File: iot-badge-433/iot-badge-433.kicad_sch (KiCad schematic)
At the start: 70 parts, among them J1 USB_C_Receptacle_USB2.0, J2 Wire ANT, J3 Conn_01x04_Male, Q1 BC847, Q2 BC847, SW1 SW_Push, SW2 SW_Push, SW3 SW_Push, SW4 SW_Push, SW5 SW_Push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

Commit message: added resistors to sw to protect against shorts
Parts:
- added R21, R22: 220, Resistor_SMD:R_0805_2012Metric_Pad1.20x1.40mm_HandSolder, symbol Device:R
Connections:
- net SW5-32: now also R21.2; no longer SW5.1
- net SW6-33: now also R22.2; no longer SW6.1
- new net: R21.1, SW5.1
- new net: R22.1, SW6.1
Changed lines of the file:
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@@
     (stroke (width 0) (type default) (color 0 0 0 0))
   )
-  (wire (pts (xy 259.08 157.48) (xy 269.24 157.48))
-    (stroke (width 0) (type default) (color 0 0 0 0))
-  )
   (wire (pts (xy 21.59 55.88) (xy 21.59 57.15))
     (stroke (width 0) (type default) (color 0 0 0 0))
@@
     (stroke (width 0) (type default) (color 0 0 0 0))
   )
+  (wire (pts (xy 259.08 157.48) (xy 260.35 157.48))
+    (stroke (width 0) (type default) (color 0 0 0 0))
+  )
   (wire (pts (xy 43.18 170.18) (xy 58.42 170.18))
     (stroke (width 0) (type default) (color 0 0 0 0))
@@
     (stroke (width 0) (type default) (color 0 0 0 0))
   )
-  (wire (pts (xy 259.08 146.05) (xy 269.24 146.05))
-    (stroke (width 0) (type default) (color 0 0 0 0))
-  )
   (wire (pts (xy 29.21 44.45) (xy 29.21 45.72))
     (stroke (width 0) (type default) (color 0 0 0 0))
@@
     (stroke (width 0) (type default) (color 0 0 0 0))
   )
+  (wire (pts (xy 259.08 146.05) (xy 260.35 146.05))
+    (stroke (width 0) (type default) (color 0 0 0 0))
+  )
   (wire (pts (xy 205.74 157.48) (xy 205.74 158.75))
     (stroke (width 0) (type default) (color 0 0 0 0))
@@
     (stroke (width 0) (type default) (color 0 0 0 0))
   )
+  (wire (pts (xy 267.97 157.48) (xy 269.24 157.48))
+    (stroke (width 0) (type default) (color 0 0 0 0))
+  )
   (wire (pts (xy 250.19 34.29) (xy 254 34.29))
     (stroke (width 0) (type default) (color 0 0 0 0))
@@
     (stroke (width 0) (type default) (color 0 0 0 0))
   )
+  (wire (pts (xy 267.97 146.05) (xy 269.24 146.05))
+    (stroke (width 0) (type default) (color 0 0 0 0))
+  )
   (wire (pts (xy 147.32 176.53) (xy 147.32 167.64))
     (stroke (width 0) (type default) (color 0 0 0 0))
@@
     (pin "2")
   )
+  (symbol (lib_id "Device:R") (at 264.16 157.48 270) (unit 1)
+    (in_bom yes) (on_board yes) (fields_autoplaced)
+    (property "Reference" "R22" (id 0) (at 264.16 151.13 90))
+    (property "Value" "220" (id 1) (at 264.16 153.67 90))
+    (property "Footprint" "Resistor_SMD:R_0805_2012Metric_Pad1.20x1.40mm_HandSolder" (id 2) (at 264.16 155.702 90)
+      (effects (font (size 1.27 1.27)) hide)
+    )
+    (property "Datasheet" "~" (id 3) (at 264.16 157.48 0)
+      (effects (font (size 1.27 1.27)) hide)
+    )
+    (pin "1")
+    (pin "2")
+  )
   (symbol (lib_id "power:Earth") (at 205.74 158.75 0) (unit 1)
     (in_bom yes) (on_board yes) (fields_autoplaced)
@@
     (pin "2")
   )
+  (symbol (lib_id "Device:R") (at 264.16 146.05 270) (unit 1)
+    (in_bom yes) (on_board yes) (fields_autoplaced)
+    (property "Reference" "R21" (id 0) (at 264.16 139.7 90))
+    (property "Value" "220" (id 1) (at 264.16 142.24 90))
+    (property "Footprint" "Resistor_SMD:R_0805_2012Metric_Pad1.20x1.40mm_HandSolder" (id 2) (at 264.16 144.272 90)
+      (effects (font (size 1.27 1.27)) hide)
+    )
+    (property "Datasheet" "~" (id 3) (at 264.16 146.05 0)
+      (effects (font (size 1.27 1.27)) hide)
+    )
+    (pin "1")
+    (pin "2")
+  )
   (symbol (lib_id "Device:LED") (at 266.7 69.85 90) (unit 1)
     (in_bom yes) (on_board yes)
@@
       (reference "R20") (unit 1) (value "20k") (footprint "Resistor_SMD:R_0805_2012Metric_Pad1.20x1.40mm_HandSolder")
     )
+    (path "/a94d6832-7d1d-42d9-9422-eb0ac2cf6b62"
+      (reference "R21") (unit 1) (value "220") (footprint "Resistor_SMD:R_0805_2012Metric_Pad1.20x1.40mm_HandSolder")
+    )
+    (path "/1cb6b24c-a887-45f3-a8f4-72a5085c9147"
+      (reference "R22") (unit 1) (value "220") (footprint "Resistor_SMD:R_0805_2012Metric_Pad1.20x1.40mm_HandSolder")
+    )
     (path "/0c62dc8b-b218-44e3-b535-1d9d37793c70"

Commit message: added resistor to switch
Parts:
- added R23: 220, Resistor_SMD:R_0805_2012Metric_Pad1.20x1.40mm_HandSolder, symbol Device:R
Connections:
- net SW4-17: now also R23.2; no longer SW4.1
- new net: R23.1, SW4.1
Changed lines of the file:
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@@
     (stroke (width 0) (type default) (color 0 0 0 0))
   )
+  (wire (pts (xy 226.06 157.48) (xy 227.33 157.48))
+    (stroke (width 0) (type default) (color 0 0 0 0))
+  )
   (wire (pts (xy 43.18 170.18) (xy 58.42 170.18))
     (stroke (width 0) (type default) (color 0 0 0 0))
@@
     (stroke (width 0) (type default) (color 0 0 0 0))
   )
-  (wire (pts (xy 217.17 157.48) (xy 227.33 157.48))
-    (stroke (width 0) (type default) (color 0 0 0 0))
-  )
   (wire (pts (xy 181.61 72.39) (xy 181.61 77.47))
     (stroke (width 0) (type default) (color 0 0 0 0))
@@
     (stroke (width 0) (type default) (color 0 0 0 0))
   )
+  (wire (pts (xy 217.17 157.48) (xy 218.44 157.48))
+    (stroke (width 0) (type default) (color 0 0 0 0))
+  )
   (wire (pts (xy 259.08 146.05) (xy 260.35 146.05))
     (stroke (width 0) (type default) (color 0 0 0 0))
@@
     (pin "3")
   )
+  (symbol (lib_id "Device:R") (at 222.25 157.48 270) (unit 1)
+    (in_bom yes) (on_board yes) (fields_autoplaced)
+    (property "Reference" "R23" (id 0) (at 222.25 151.13 90))
+    (property "Value" "220" (id 1) (at 222.25 153.67 90))
+    (property "Footprint" "Resistor_SMD:R_0805_2012Metric_Pad1.20x1.40mm_HandSolder" (id 2) (at 222.25 155.702 90)
+      (effects (font (size 1.27 1.27)) hide)
+    )
+    (property "Datasheet" "~" (id 3) (at 222.25 157.48 0)
+      (effects (font (size 1.27 1.27)) hide)
+    )
+    (pin "1")
+    (pin "2")
+  )
   (symbol (lib_id "Device:R") (at 114.3 49.53 0) (unit 1)
     (in_bom yes) (on_board yes) (fields_autoplaced)
@@
       (reference "R22") (unit 1) (value "220") (footprint "Resistor_SMD:R_0805_2012Metric_Pad1.20x1.40mm_HandSolder")
     )
+    (path "/4066045d-e6eb-4299-961f-4f291fcb9ac4"
+      (reference "R23") (unit 1) (value "220") (footprint "Resistor_SMD:R_0805_2012Metric_Pad1.20x1.40mm_HandSolder")
+    )
     (path "/0c62dc8b-b218-44e3-b535-1d9d37793c70"

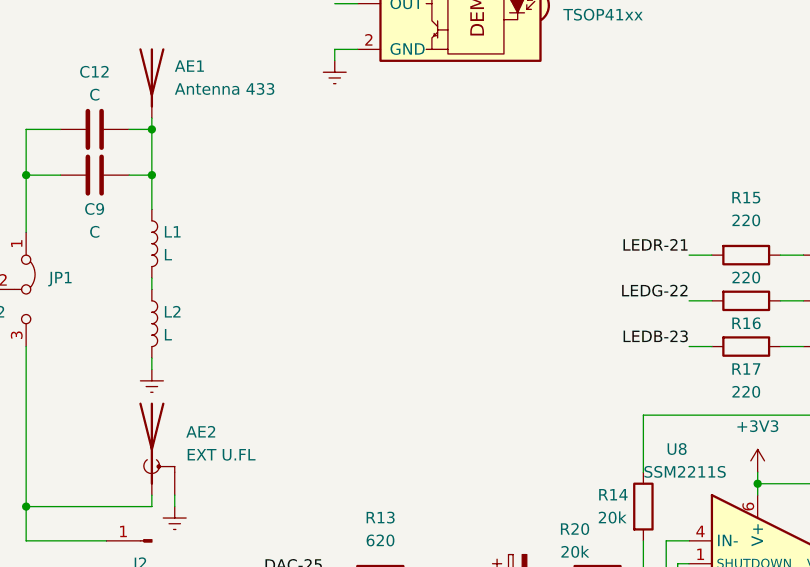
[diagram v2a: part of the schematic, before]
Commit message: added i2s mic symbol
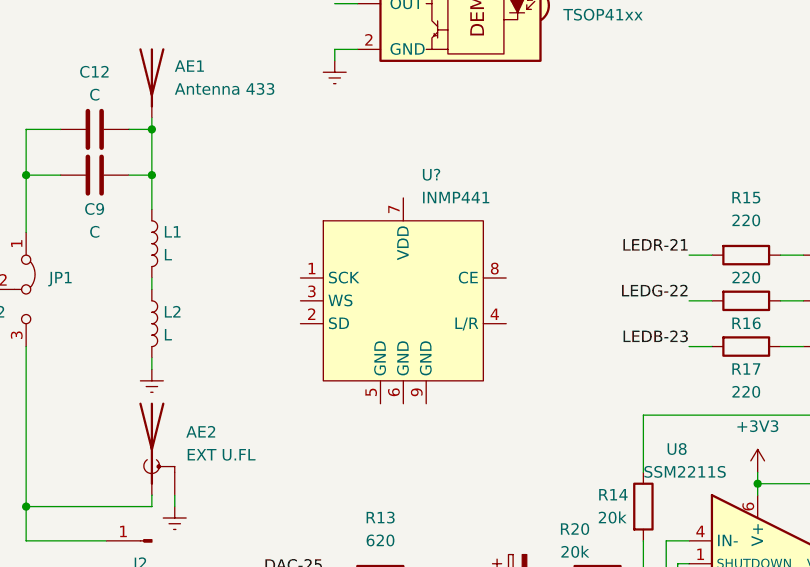
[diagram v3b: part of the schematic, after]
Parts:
- added U?: INMP441, symbol Microphone_I2S:INMP441
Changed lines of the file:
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@@
     (effects (font (size 1.27 1.27)) (justify left bottom))
+  )
+  (symbol (lib_id "Microphone_I2S:INMP441") (at 209.55 91.44 0) (unit 1)
+    (in_bom yes) (on_board yes) (fields_autoplaced)
+    (property "Reference" "U?" (id 0) (at 211.5694 77.47 0)
+      (effects (font (size 1.27 1.27)) (justify left))
+    )
+    (property "Value" "INMP441" (id 1) (at 211.5694 80.01 0)
+      (effects (font (size 1.27 1.27)) (justify left))
+    )
+    (property "Footprint" "" (id 2) (at 209.55 91.44 0)
+      (effects (font (size 1.27 1.27)) hide)
+    )
+    (property "Datasheet" "" (id 3) (at 209.55 91.44 0)
+      (effects (font (size 1.27 1.27)) hide)
+    )
+    (pin "1")
+    (pin "2")
+    (pin "3")
+    (pin "4")
+    (pin "5")
+    (pin "6")
+    (pin "7")
+    (pin "8")
+    (pin "9")
   )
   (symbol (lib_id "power:Earth") (at 46.99 189.23 0) (unit 1)
@@
       (reference "U8") (unit 1) (value "SSM2211S") (footprint "Package_SO:SOIC-8_3.9x4.9mm_P1.27mm")
     )
+    (path "/00a389a1-1c9e-4af7-8f1d-1454f7ecf142"
+      (reference "U?") (unit 1) (value "INMP441") (footprint "")
+    )
     (path "/b6bf3229-edbf-4e20-84e4-316f6abc0502"

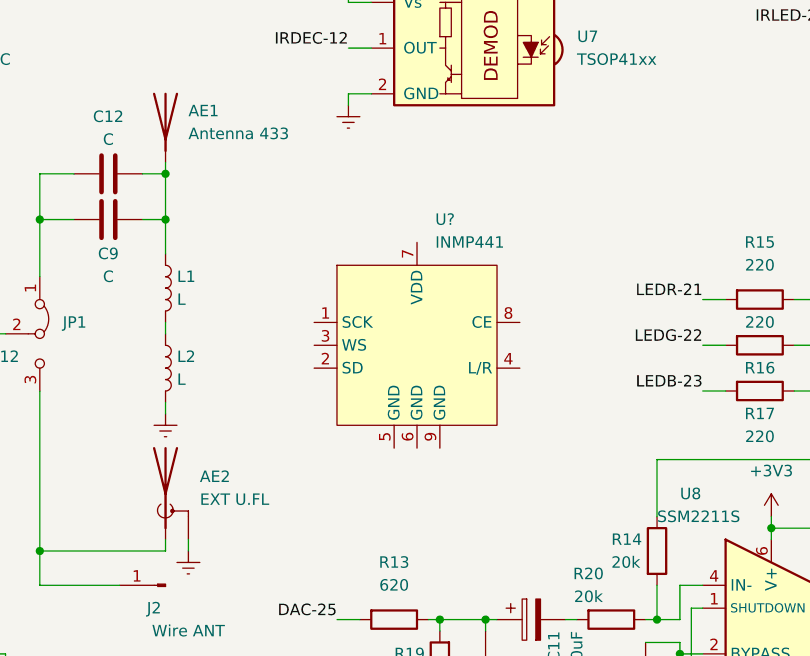
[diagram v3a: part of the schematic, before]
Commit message: placed i2c mic in pcb
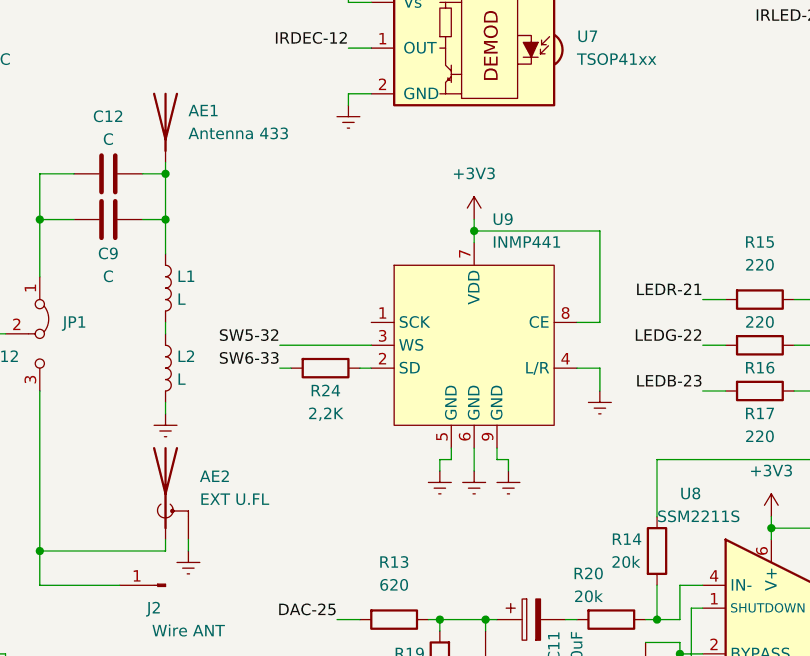
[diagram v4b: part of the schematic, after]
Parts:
- added R24: 2,2K, Resistor_SMD:R_0805_2012Metric_Pad1.20x1.40mm_HandSolder, symbol Device:R
- U9: renamed from U?; footprint (none) -> Microphone_I2S:INMP441
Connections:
- net +3V3: now also U9.7 (VDD), U9.8 (CE)
- net Earth: now also U9.4 (L/R), U9.5 (GND), U9.6 (GND), U9.9 (GND)
- net SW5-32: now also U9.3 (WS)
- net SW6-33: now also R24.2
- net at U9.2 (SD): now also R24.1
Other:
- moved on the sheet: U9

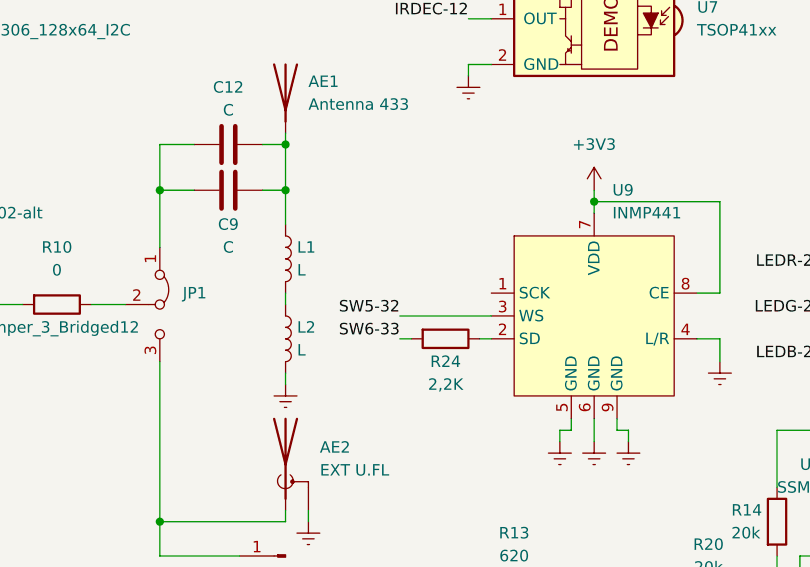
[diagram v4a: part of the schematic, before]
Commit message: finished placing i2s mic
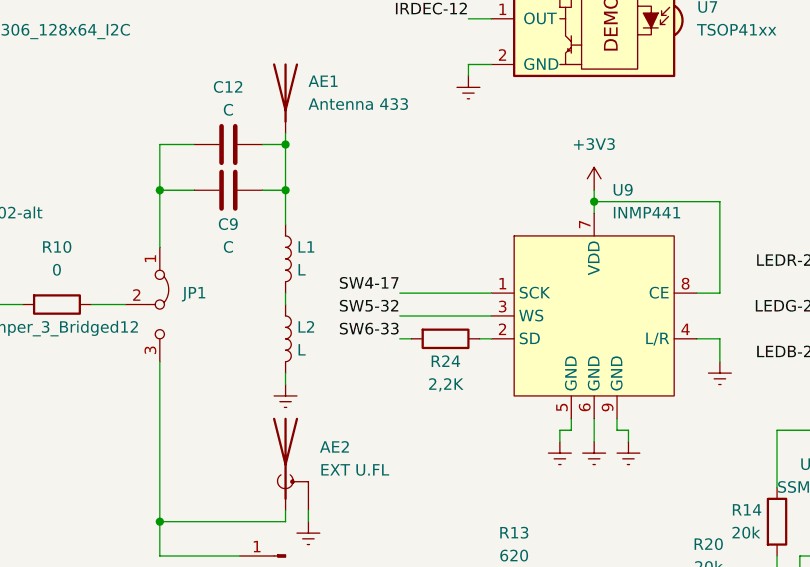
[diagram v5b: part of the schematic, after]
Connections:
- net SW4-17: now also U9.1 (SCK)
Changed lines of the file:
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@@
+    (stroke (width 0) (type default) (color 0 0 0 0))
+  )
+  (wire (pts (xy 194.31 88.9) (xy 204.47 88.9))
     (stroke (width 0) (type default) (color 0 0 0 0))
   )
@@
     (effects (font (size 1.27 1.27)) (justify left bottom))
   )
+  (label "SW4-17" (at 194.31 88.9 180)
+    (effects (font (size 1.27 1.27)) (justify right bottom))
+  )
   (label "SW6-33" (at 259.08 157.48 180)
